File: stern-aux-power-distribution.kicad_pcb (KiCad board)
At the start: 2 copper layers, 50 x 36 mm, 10 parts, among them J1 Conn_01x04, J2 Conn_01x02_Pin, J3 Conn_01x02_Pin, J4 Conn_01x02_Pin, J5 Conn_01x02_Pin

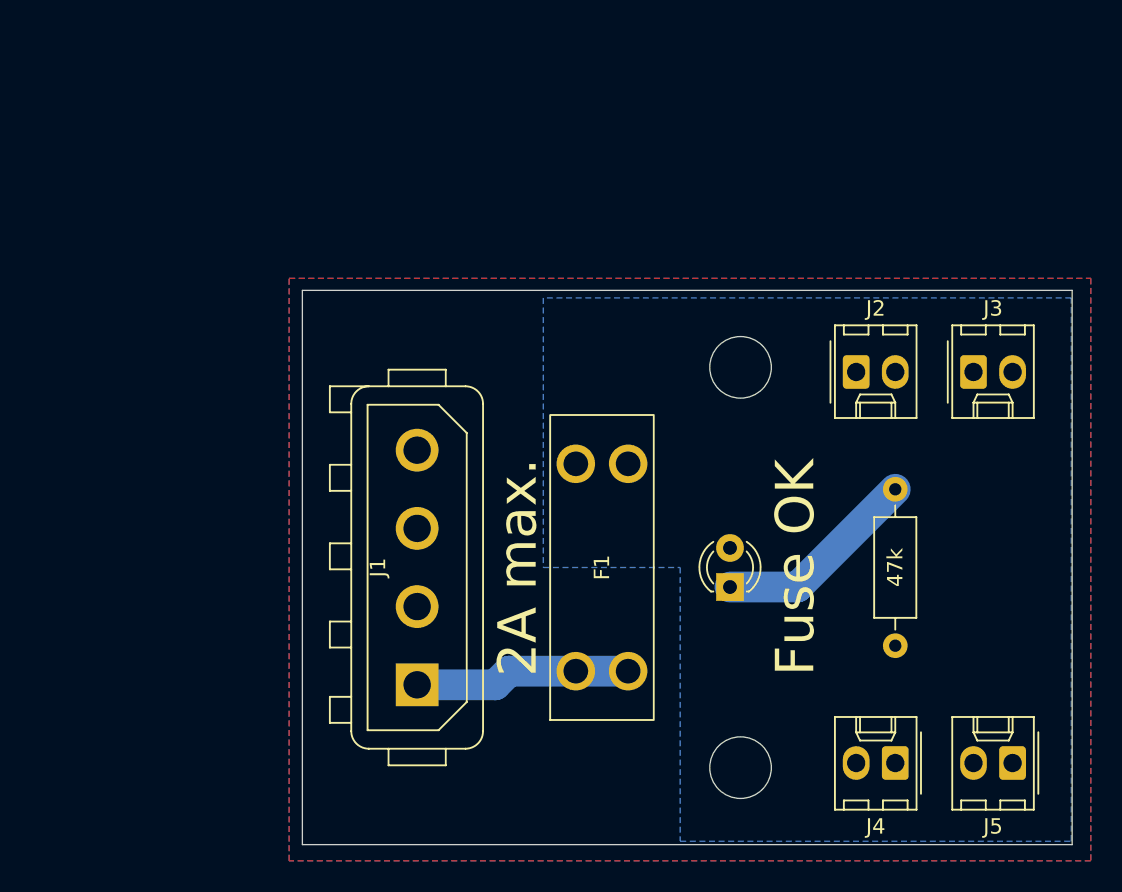
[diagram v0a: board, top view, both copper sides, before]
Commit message: More silkscreen info
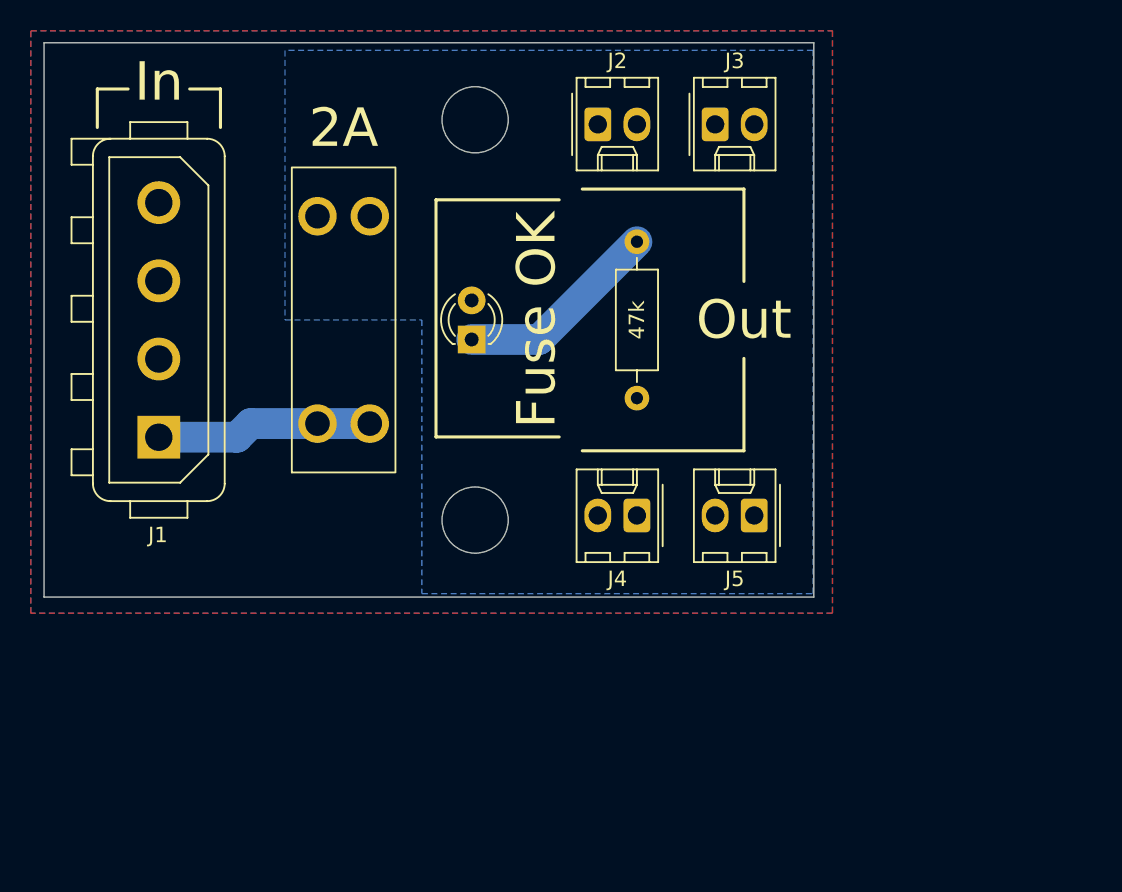
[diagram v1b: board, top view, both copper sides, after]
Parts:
- H1, H2: footprint MountingHole:MountingHole_4mm -> MountingHole:MountingHole_4.3mm_M4
- moved H1 23.6 mm to (42.6, 45.2)
- moved H2 23.6 mm to (42.6, 19.2)
- moved J1 23.2 mm to (22.0, 39.8)
- moved J3 23.2 mm to (58.1, 19.5)
- moved D1 23.2 mm to (42.3, 33.5)
- moved J2 23.2 mm to (50.5, 19.5)
- moved J5 23.2 mm to (60.7, 44.9)
- moved F1 23.2 mm to (34.0, 32.2)
- moved J4 23.2 mm to (53.1, 44.9)
- moved R1 23.2 mm to (53.1, 27.1)
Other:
- board text added: "2A"
- board text added: "ATX standard connection"
- board text added: "Aux power distribution for Stern machines Rev 1"
- board text added: "Hendrik Leibrandt https://github.com/Ardenryst/stern-aux-power-distribution"
- board text added: "In"
- board text added: "Out"
- board text removed: "2A max."
- board text removed: "Aux power distribution for Stern machines"
